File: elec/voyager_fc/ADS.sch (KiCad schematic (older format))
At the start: 2 parts

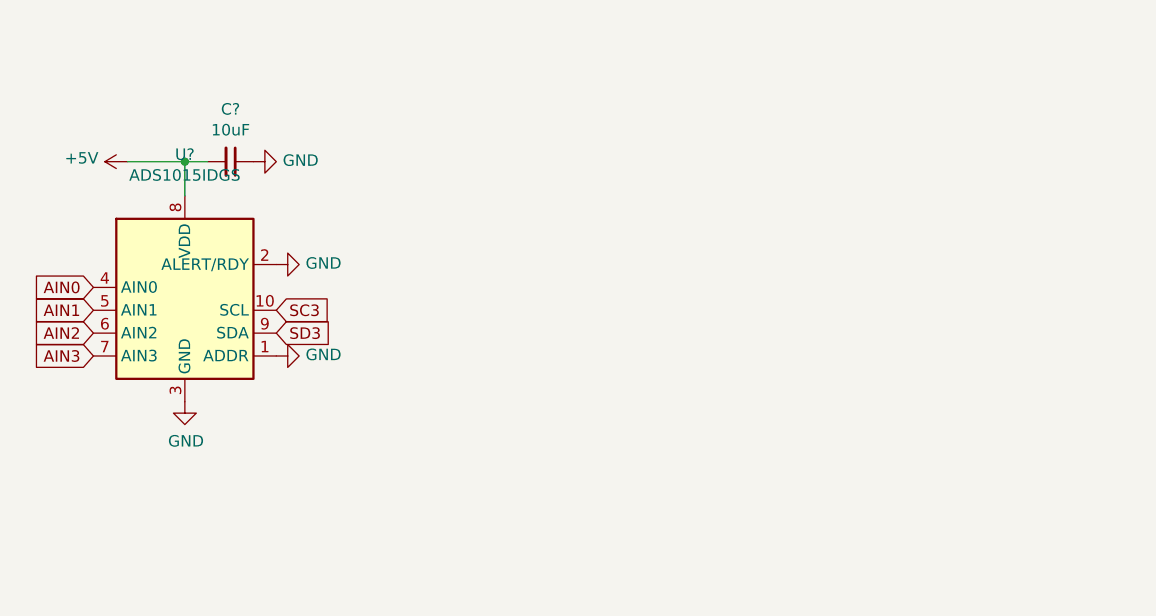
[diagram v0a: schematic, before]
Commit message: Move connectors inside schematics
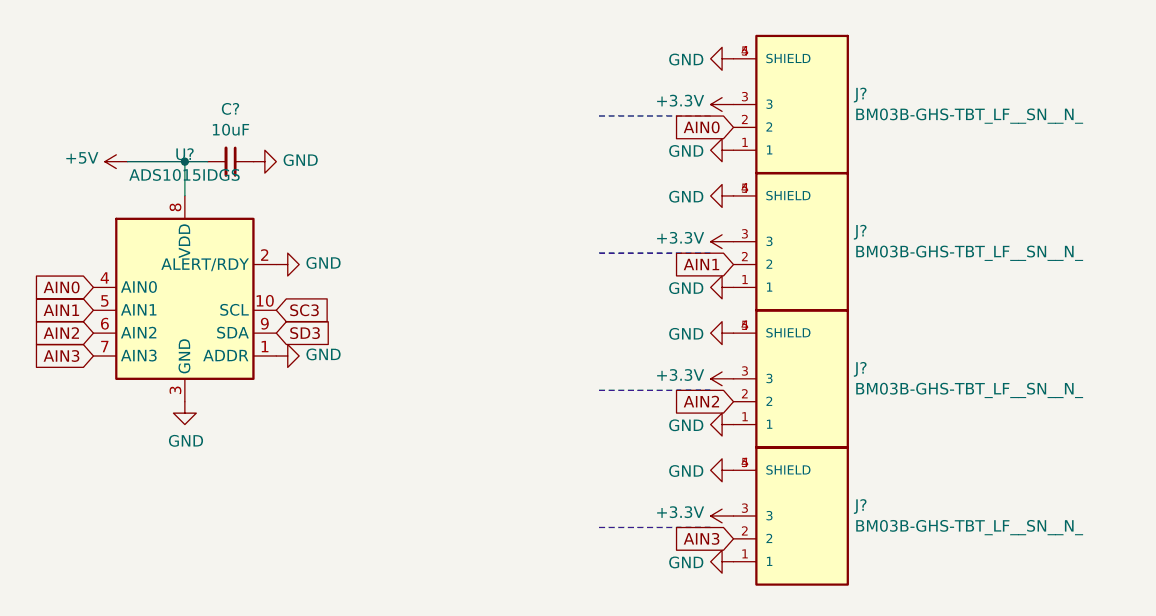
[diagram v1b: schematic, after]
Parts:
- added J? (x4): BM03B-GHS-TBT_LF__SN__N_, CONN_BM03B-GHS-TBT_LF__SN__N_, symbol BM03B-GHS-TBT_LF__SN__N_:BM03B-GHS-TBT_LF__SN__N_
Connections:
- net AIN0: now also J?.2
- net AIN1: now also J?.2
- net AIN2: now also J?.2
- net AIN3: now also J?.2
- net GND: now also J?.1, J?.1, J?.1, J?.1, J?.4 (SHIELD), J?.4 (SHIELD), J?.4 (SHIELD), J?.4 (SHIELD), J?.5 (SHIELD), J?.5 (SHIELD), J?.5 (SHIELD), J?.5 (SHIELD)
- new net +3V3: J?.3, J?.3, J?.3, J?.3

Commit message: Place all components and start route
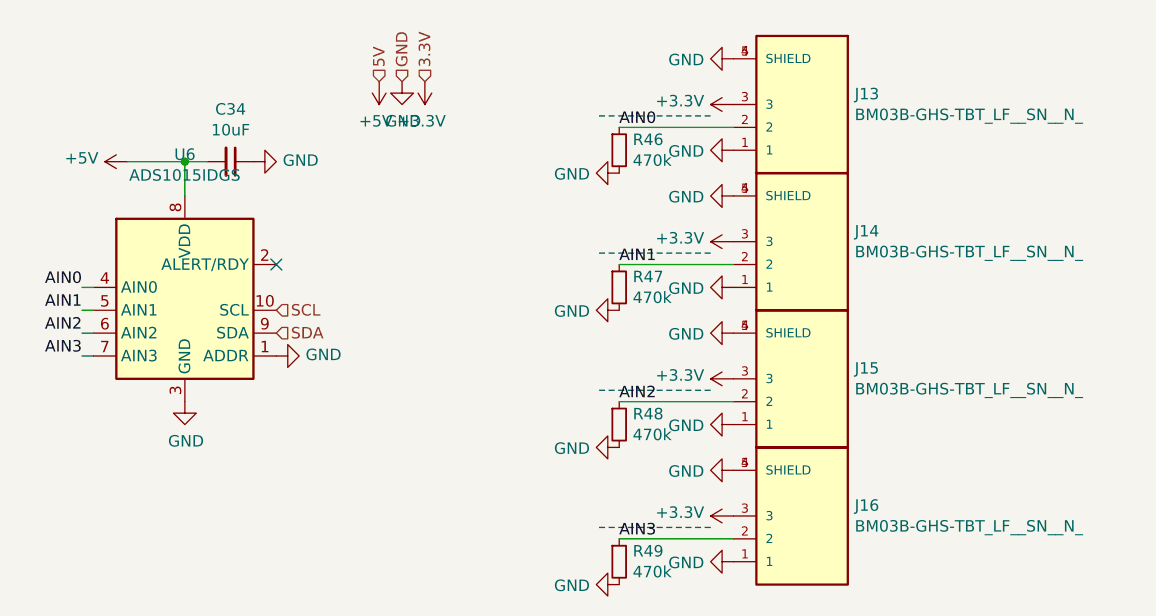
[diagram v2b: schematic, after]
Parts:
- added R46, R47, R48, R49: 470k, Resistor_SMD:R_0603_1608Metric, symbol Device:R_Small
- C34: renamed from C?; footprint Capacitor_SMD:C_0805_2012Metric -> Capacitor_SMD:C_0603_1608Metric
- J13, J14, J15, J16: renamed from J?; footprint CONN_BM03B-GHS-TBT_LF__SN__N_ -> BM03B-GHS-TBT_LF__SN__N_:CONN_BM03B-GHS-TBT_LF__SN__N_
- gave numbers to parts that had none: 1
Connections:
- net AIN0: now also R46.1
- net AIN1: now also R47.1
- net AIN2: now also R48.1
- net AIN3: now also R49.1
- net GND: now also R46.2, R47.2, R48.2, R49.2; no longer U6.2 (ALERT/RDY)
- net SC3 renamed SCL
- net SD3 renamed SDA
- no-connect marks 0 -> 1
